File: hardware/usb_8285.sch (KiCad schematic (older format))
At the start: 20 parts, among them P1 UTX, P2 URX, P3 D+, P4 +5V, P5 +5V, P6 GND, P7 GND, P8 D-, P9 G0, U1 ESP8266EX, U2 MCP1824, X1 26MHz

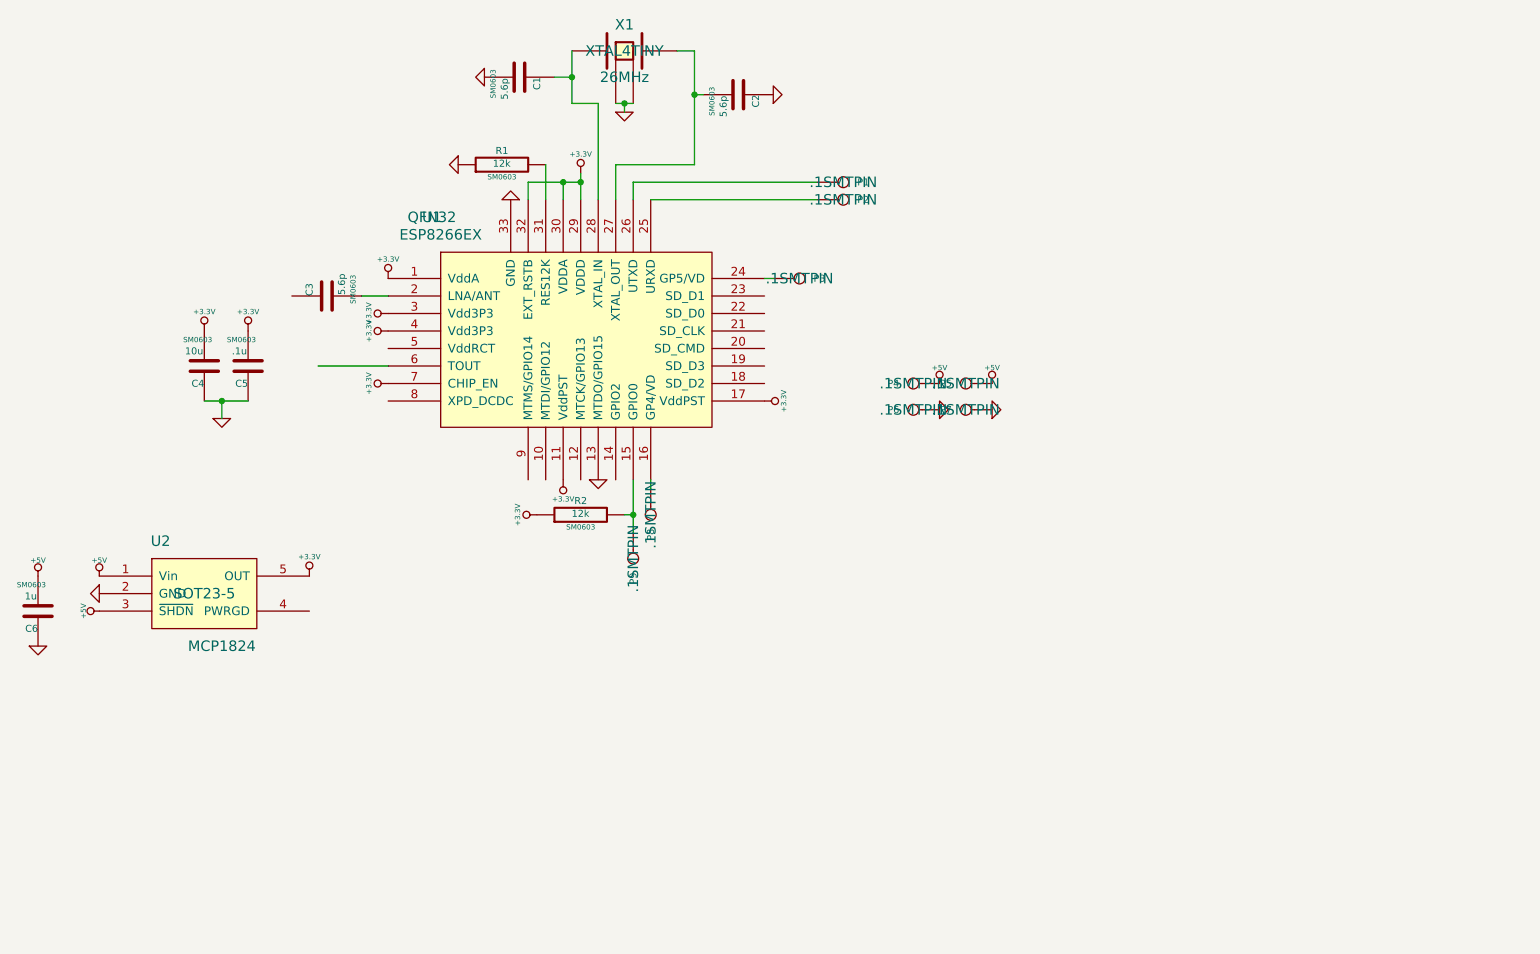
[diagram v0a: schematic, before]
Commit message: Add Schematic updates.  Add a ton of comments in the ASM, optimize more for size, since speed on usb 1.1 low speed is sufficient.
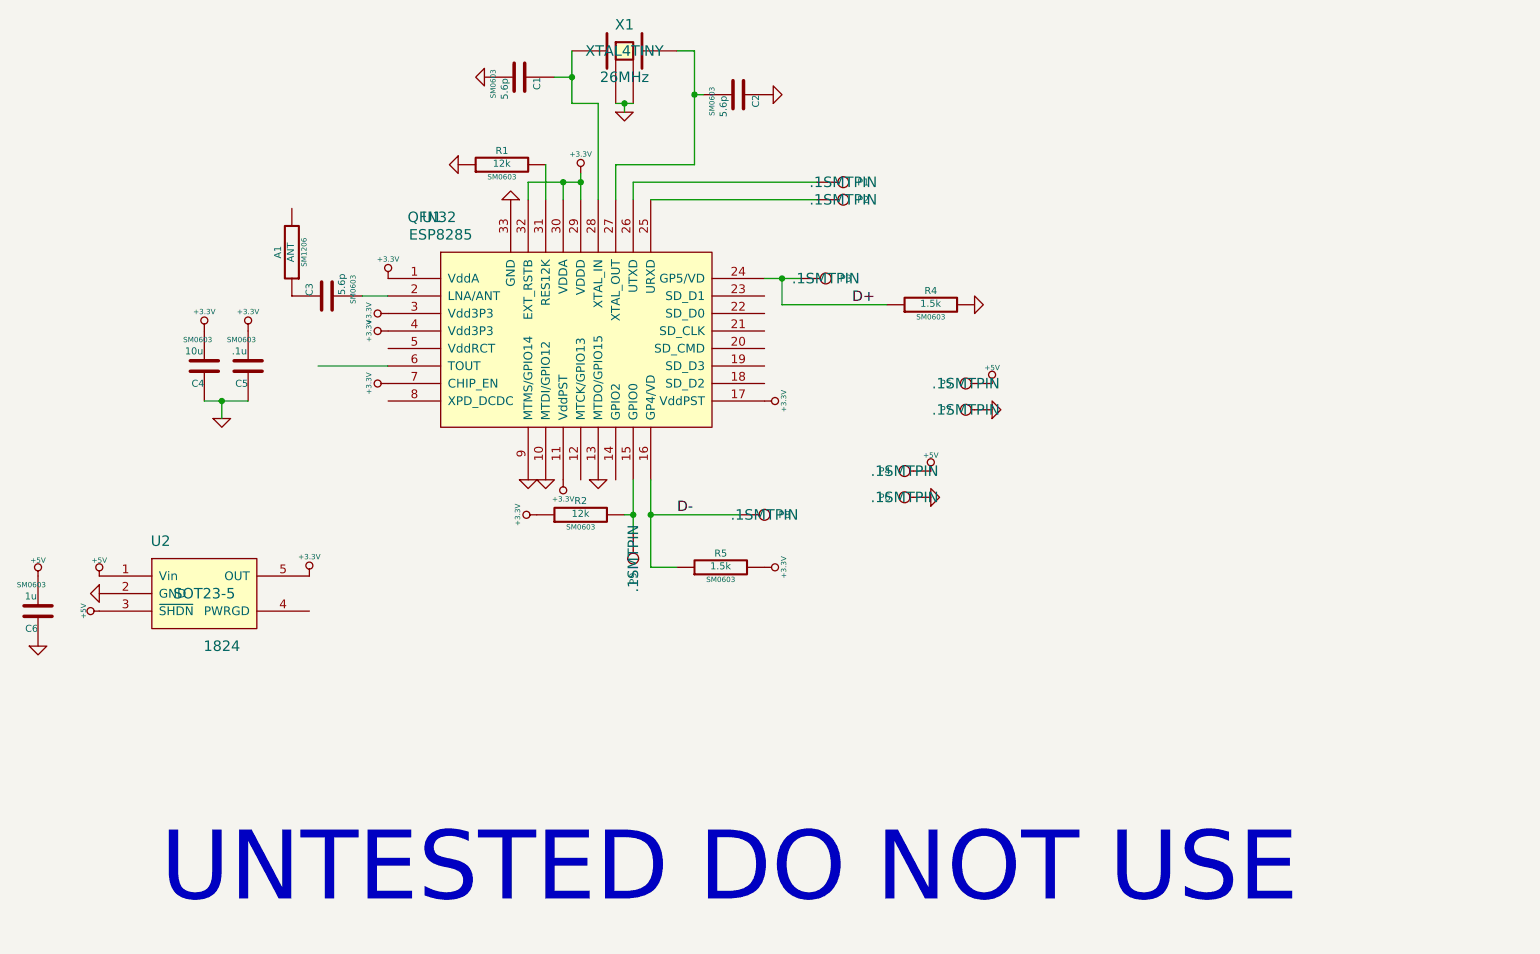
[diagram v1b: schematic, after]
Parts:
- added A1: ANT, SM1206, symbol R
- added R4, R5: 1.5k, SM0603, symbol R
- U1: value ESP8266EX -> ESP8285
- U2: value MCP1824 -> 1824
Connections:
- net labels added: D+, D-
- wire segments 27 -> 31
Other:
- note added: "UNTESTED DO NOT USE"
- moved on the sheet: P3, P4, P6, P8
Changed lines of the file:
@@
 LIBS:23lc1024
 LIBS:2.4GHZ_2450FB15L0001
+LIBS:usb_8285-cache
 EELAYER 27 0
 EELAYER END
@@
 Sheet 1 1
 Title "noname.sch"
-Date "3 aug 2016"
+Date "8 aug 2016"
 Rev "-"
 Comp ""
@@
 P 4550 2400
 F 0 "U1" H 3650 3100 60  0000 C CNN
-F 1 "ESP8266EX" H 3700 3000 60  0000 C CNN
+F 1 "ESP8285" H 3700 3000 60  0000 C CNN
 F 2 "QFN32" H 3650 3100 60  0000 C CNN
 F 3 "~" H 3650 3100 60  0000 C CNN
@@
 L CONN_1 P3
 U 1 1 57A262F1
-P 5750 2050
-F 0 "P3" H 5830 2050 40  0000 L CNN
-F 1 "D+" H 5750 2105 30  0001 C CNN
-F 2 ".1SMTPIN" H 5750 2050 60  0000 C CNN
-F 3 "" H 5750 2050 60  0000 C CNN
-	1    5750 2050
+P 5900 2050
+F 0 "P3" H 5980 2050 40  0000 L CNN
+F 1 "D+" H 5900 2105 30  0001 C CNN
+F 2 ".1SMTPIN" H 5900 2050 60  0000 C CNN
+F 3 "" H 5900 2050 60  0000 C CNN
+	1    5900 2050
 	1    0    0    -1
 $EndComp
@@
 L CONN_1 P8
 U 1 1 57A262FE
-P 4900 3400
-F 0 "P8" H 4980 3400 40  0000 L CNN
-F 1 "D-" H 4900 3455 30  0001 C CNN
-F 2 ".1SMTPIN" H 4900 3400 60  0000 C CNN
-F 3 "" H 4900 3400 60  0000 C CNN
-	1    4900 3400
-	0    1    1    0
-$EndComp
-Wire Wire Line
-	4900 3200 4900 3250
+P 5550 3400
+F 0 "P8" H 5630 3400 40  0000 L CNN
+F 1 "D-" H 5550 3455 30  0001 C CNN
+F 2 ".1SMTPIN" H 5550 3400 60  0000 C CNN
+F 3 "" H 5550 3400 60  0000 C CNN
+	1    5550 3400
+	1    0    0    -1
+$EndComp
+Wire Wire Line
+	4900 3200 4900 3700
 $Comp
 L CONN_1 P4
 U 1 1 57A26363
-P 6400 2650
-F 0 "P4" H 6480 2650 40  0000 L CNN
-F 1 "+5V" H 6400 2705 30  0001 C CNN
-F 2 ".1SMTPIN" H 6400 2650 60  0000 C CNN
-F 3 "" H 6400 2650 60  0000 C CNN
-	1    6400 2650
+P 6350 3150
+F 0 "P4" H 6430 3150 40  0000 L CNN
+F 1 "+5V" H 6350 3205 30  0001 C CNN
+F 2 ".1SMTPIN" H 6350 3150 60  0000 C CNN
+F 3 "" H 6350 3150 60  0000 C CNN
+	1    6350 3150
 	-1   0    0    1
 $EndComp
@@
 L CONN_1 P6
 U 1 1 57A2636F
-P 6400 2800
-F 0 "P6" H 6480 2800 40  0000 L CNN
-F 1 "GND" H 6400 2855 30  0001 C CNN
-F 2 ".1SMTPIN" H 6400 2800 60  0000 C CNN
-F 3 "" H 6400 2800 60  0000 C CNN
-	1    6400 2800
+P 6350 3300
+F 0 "P6" H 6430 3300 40  0000 L CNN
+F 1 "GND" H 6350 3355 30  0001 C CNN
+F 2 ".1SMTPIN" H 6350 3300 60  0000 C CNN
+F 3 "" H 6350 3300 60  0000 C CNN
+	1    6350 3300
 	-1   0    0    1
 $EndComp
@@
 L GND #PWR014
 U 1 1 57A26375
-P 6550 2800
-F 0 "#PWR014" H 6550 2800 30  0001 C CNN
-F 1 "GND" H 6550 2730 30  0001 C CNN
-F 2 "" H 6550 2800 60  0000 C CNN
-F 3 "" H 6550 2800 60  0000 C CNN
-	1    6550 2800
-	0    -1   -1   0
-$EndComp
-Wire Wire Line
-	5600 2050 5550 2050
+P 6500 3300
+F 0 "#PWR014" H 6500 3300 30  0001 C CNN
+F 1 "GND" H 6500 3230 30  0001 C CNN
+F 2 "" H 6500 3300 60  0000 C CNN
+F 3 "" H 6500 3300 60  0000 C CNN
+	1    6500 3300
+	0    -1   -1   0
+$EndComp
+Wire Wire Line
+	5550 2050 5750 2050
 $Comp
 L CONN_1 P1
@@
 L +5V #PWR016
 U 1 1 57A26469
-P 6550 2650
-F 0 "#PWR016" H 6550 2740 20  0001 C CNN
-F 1 "+5V" H 6550 2740 30  0000 C CNN
-F 2 "" H 6550 2650 60  0000 C CNN
-F 3 "" H 6550 2650 60  0000 C CNN
-	1    6550 2650
+P 6500 3150
+F 0 "#PWR016" H 6500 3240 20  0001 C CNN
+F 1 "+5V" H 6500 3240 30  0000 C CNN
+F 2 "" H 6500 3150 60  0000 C CNN
+F 3 "" H 6500 3150 60  0000 C CNN
+	1    6500 3150
 	1    0    0    -1
 $EndComp
@@
 P 2350 3850
 F 0 "U2" H 2100 4150 60  0000 C CNN
-F 1 "MCP1824" H 2450 3550 60  0000 C CNN
+F 1 "1824" H 2450 3550 60  0000 C CNN
 F 2 "SOT23-5" H 2350 3850 60  0000 C CNN
 F 3 "" H 2350 3850 60  0000 C CNN
@@
 	1    0    0    -1
 $EndComp
+Text Notes 2100 5650 0    394  ~ 0
+UNTESTED DO NOT USE
+$Comp
+L R A1
+U 1 1 57A8E837
+P 2850 1900
+F 0 "A1" V 2930 1900 40  0000 C CNN
+F 1 "ANT" V 2857 1901 40  0000 C CNN
+F 2 "SM1206" V 2780 1900 30  0000 C CNN
+F 3 "~" H 2850 1900 30  0000 C CNN
+F 4 "1292-1035-1-ND" V 2850 1900 60  0001 C CNN "Digikey"
+F 5 ".521" V 2850 1900 60  0001 C CNN "Cost10"
+	1    2850 1900
+	-1   0    0    1
+$EndComp
+$Comp
+L GND #PWR028
+U 1 1 57A8F089
+P 4200 3200
+F 0 "#PWR028" H 4200 3200 30  0001 C CNN
+F 1 "GND" H 4200 3130 30  0001 C CNN
+F 2 "" H 4200 3200 60  0000 C CNN
+F 3 "" H 4200 3200 60  0000 C CNN
+	1    4200 3200
+	1    0    0    -1
+$EndComp
+$Comp
+L GND #PWR029
+U 1 1 57A8F08F
+P 4300 3200
+F 0 "#PWR029" H 4300 3200 30  0001 C CNN
+F 1 "GND" H 4300 3130 30  0001 C CNN
+F 2 "" H 4300 3200 60  0000 C CNN
+F 3 "" H 4300 3200 60  0000 C CNN
+	1    4300 3200
+	1    0    0    -1
+$EndComp
+$Comp
+L R R4
+U 1 1 57A8F4F8
+P 6500 2200
+F 0 "R4" V 6580 2200 40  0000 C CNN
+F 1 "1.5k" V 6507 2201 40  0000 C CNN
+F 2 "SM0603" V 6430 2200 30  0000 C CNN
+F 3 "~" H 6500 2200 30  0000 C CNN
+	1    6500 2200
+	0    -1   -1   0
+$EndComp
+Wire Wire Line
+	6250 2200 5650 2200
+Wire Wire Line
+	5650 2200 5650 2050
+Connection ~ 5650 2050
+Text Label 6050 2200 0    59   ~ 0
+D+
+$Comp
+L R R5
+U 1 1 57A8F67C
+P 5300 3700
+F 0 "R5" V 5380 3700 40  0000 C CNN
+F 1 "1.5k" V 5307 3701 40  0000 C CNN
+F 2 "SM0603" V 5230 3700 30  0000 C CNN
+F 3 "~" H 5300 3700 30  0000 C CNN
+	1    5300 3700
+	0    -1   -1   0
+$EndComp
+$Comp
+L +3.3V #PWR030
+U 1 1 57A8F682
+P 5550 3700
+F 0 "#PWR030" H 5550 3660 30  0001 C CNN
+F 1 "+3.3V" H 5550 3810 30  0000 C CNN
+F 2 "" H 5550 3700 60  0000 C CNN
+F 3 "" H 5550 3700 60  0000 C CNN
+	1    5550 3700
+	0    1    1    0
+$EndComp
+$Comp
+L GND #PWR031
+U 1 1 57A8F688
+P 6750 2200
+F 0 "#PWR031" H 6750 2200 30  0001 C CNN
+F 1 "GND" H 6750 2130 30  0001 C CNN
+F 2 "" H 6750 2200 60  0000 C CNN
+F 3 "" H 6750 2200 60  0000 C CNN
+	1    6750 2200
+	0    -1   -1   0
+$EndComp
+Wire Wire Line
+	4900 3400 5400 3400
+Wire Wire Line
+	4900 3700 5050 3700
+Connection ~ 4900 3400
+Text Label 5050 3400 0    59   ~ 0
+D-
 $EndSCHEMATC

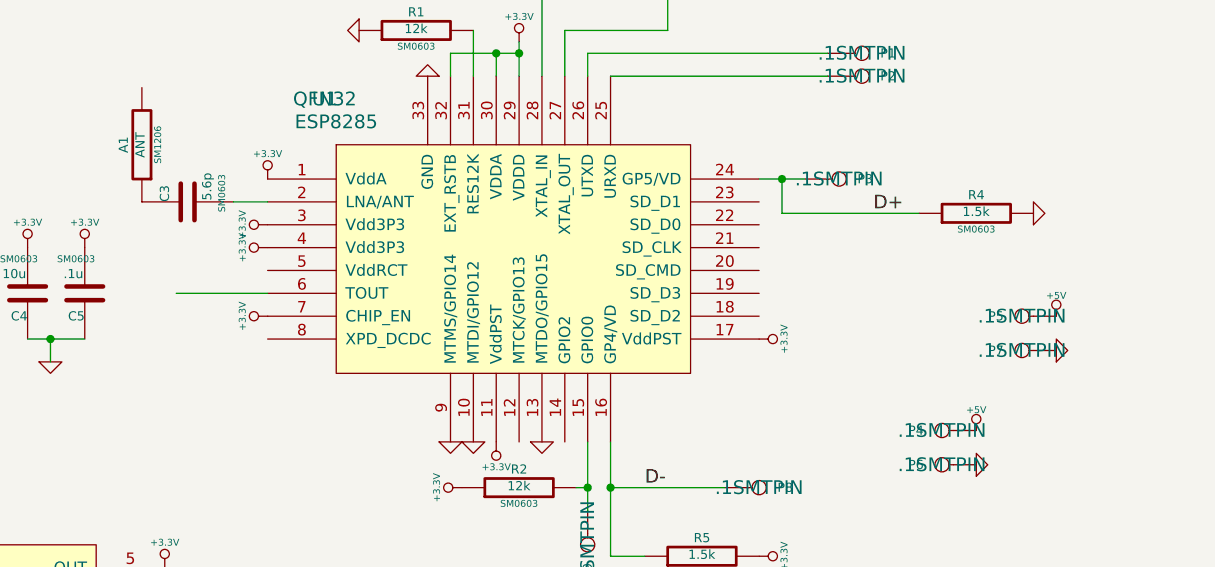
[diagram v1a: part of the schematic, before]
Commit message: update design to what I actually ordered
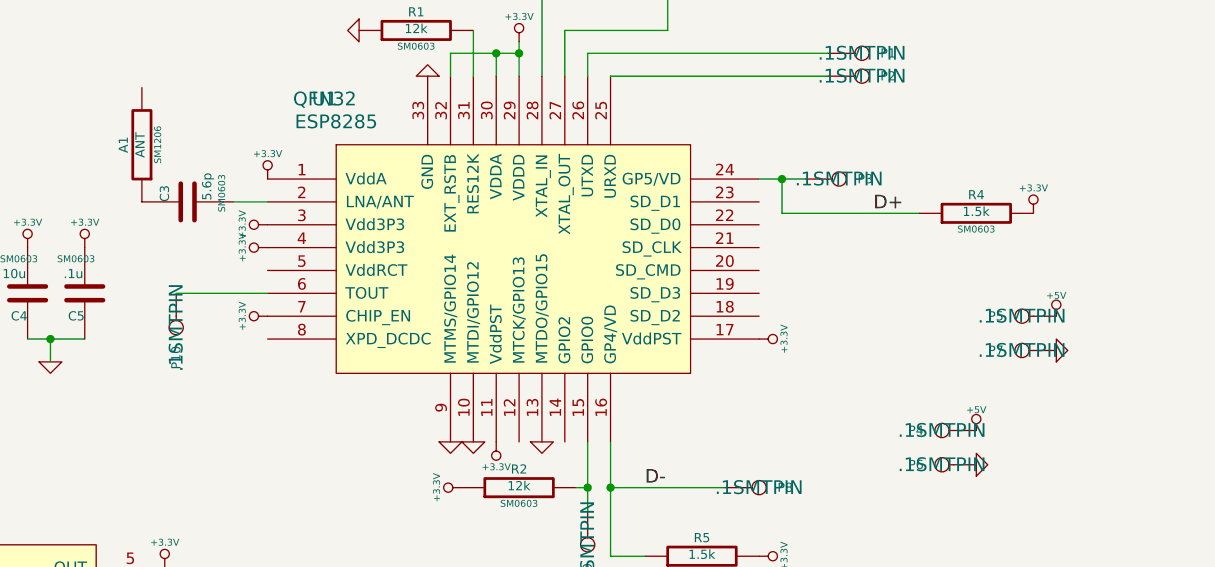
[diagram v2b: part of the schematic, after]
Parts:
- added P10: ADC, .1SMTPIN, symbol CONN_1
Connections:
- net +3.3V: now also R4.2
- net GND: no longer R4.2
- net at U1.6 (TOUT): now also P10.1
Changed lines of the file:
@@
 Sheet 1 1
 Title "noname.sch"
-Date "8 aug 2016"
+Date "15 aug 2016"
 Rev "-"
 Comp ""
@@
 	0    1    1    0
 $EndComp
-$Comp
-L GND #PWR031
-U 1 1 57A8F688
-P 6750 2200
-F 0 "#PWR031" H 6750 2200 30  0001 C CNN
-F 1 "GND" H 6750 2130 30  0001 C CNN
-F 2 "" H 6750 2200 60  0000 C CNN
-F 3 "" H 6750 2200 60  0000 C CNN
-	1    6750 2200
-	0    -1   -1   0
-$EndComp
 Wire Wire Line
 	4900 3400 5400 3400
@@
 Text Label 5050 3400 0    59   ~ 0
 D-
+$Comp
+L CONN_1 P10
+U 1 1 57B2119E
+P 3000 2700
+F 0 "P10" H 3080 2700 40  0000 L CNN
+F 1 "ADC" H 3000 2755 30  0001 C CNN
+F 2 ".1SMTPIN" H 3000 2700 60  0000 C CNN
+F 3 "" H 3000 2700 60  0000 C CNN
+	1    3000 2700
+	0    1    1    0
+$EndComp
+$Comp
+L +3.3V #PWR031
+U 1 1 57B211DF
+P 6750 2200
+F 0 "#PWR031" H 6750 2160 30  0001 C CNN
+F 1 "+3.3V" H 6750 2310 30  0000 C CNN
+F 2 "" H 6750 2200 60  0000 C CNN
+F 3 "" H 6750 2200 60  0000 C CNN
+	1    6750 2200
+	1    0    0    -1
+$EndComp
 $EndSCHEMATC
